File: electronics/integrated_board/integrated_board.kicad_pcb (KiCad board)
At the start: 2 copper layers, 98.5 x 111 mm, 67 parts, among them CON1 BARREL_JACK, J1 rot_encoderZ(35,34), J10 pcf8575 IO expander, J11 Switch 1, J13 motor1(15,2,0,4), J15 motor2 (16,17,5,18), J17 motor3 (19,21,22,23), J2 rot_encoderY(25,26), J3 rot_encoderX(14,27), J4 Switch 2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

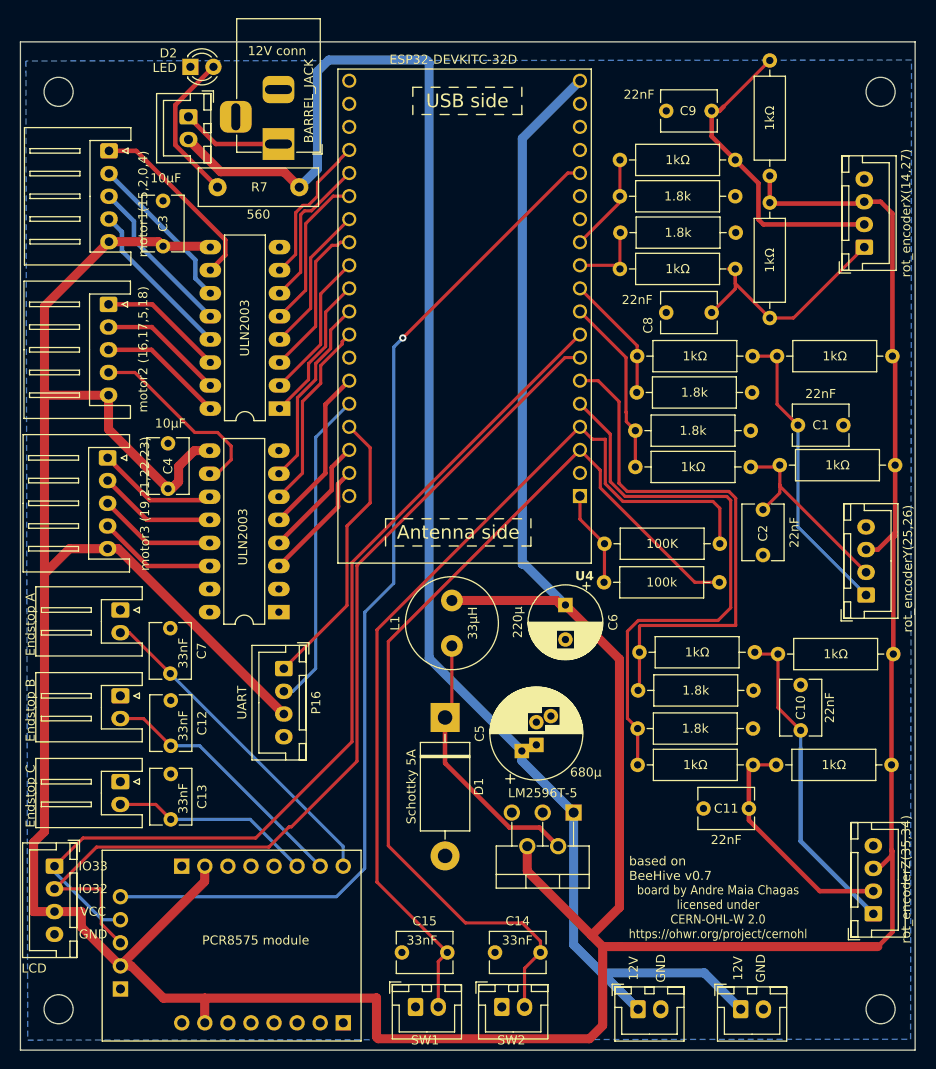
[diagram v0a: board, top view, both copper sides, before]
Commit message: Updated PCB
reintroduced voltage divider for switch 1 and 2 as pull up
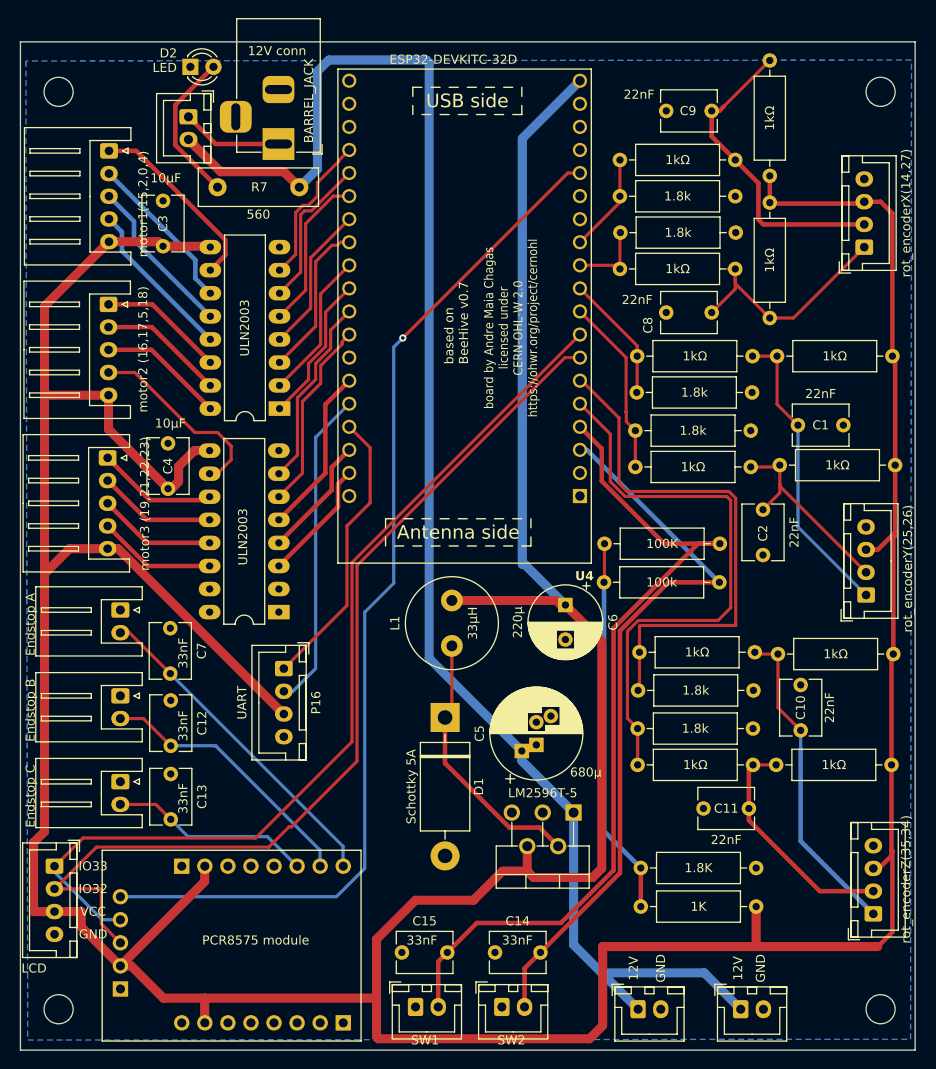
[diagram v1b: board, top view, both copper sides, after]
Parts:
- added R16: 1K, Resistor_THT:R_Axial_DIN0309_L9.0mm_D3.2mm_P12.70mm_Horizontal, F.Cu at (175.5, 135.2)
- added R17: 1.8K, Resistor_THT:R_Axial_DIN0309_L9.0mm_D3.2mm_P12.70mm_Horizontal, F.Cu at (162.8, 130.9)
- C14, C15: value C -> 33nF
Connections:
- R8 pad 2: +3V3 -> Net-(R16-Pad2)
- R9 pad 1: +3V3 -> Net-(R16-Pad2)
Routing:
- net Net-(R16-Pad2): track 0.00 -> 41.6 mm
- net Net-(J4-Pin_2): track 103.9 -> 80.3 mm
- net +5V: track 517.4 -> 535.6 mm
- net +3V3: track 10.6 -> 0.00 mm
- net Net-(J11-Pin_2): track 102.6 -> 93.5 mm
- net encoderZ_1: track 59.5 -> 58.5 mm
- net Net-(J6-Pin_2): track 28.7 -> 29.7 mm

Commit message: Updated endstop protocol
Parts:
- J10: moved to F.Cu
- moved J10 10.3 mm to (105.5, 134.0)
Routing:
- net +5V: track 535.6 -> 552.7 mm
- net I2C_SCL: track 103.7 -> 113.0 mm
- net I2C_INT: track 115.4 -> 119.6 mm
- net I2C_SDA: track 106.6 -> 105.6 mm

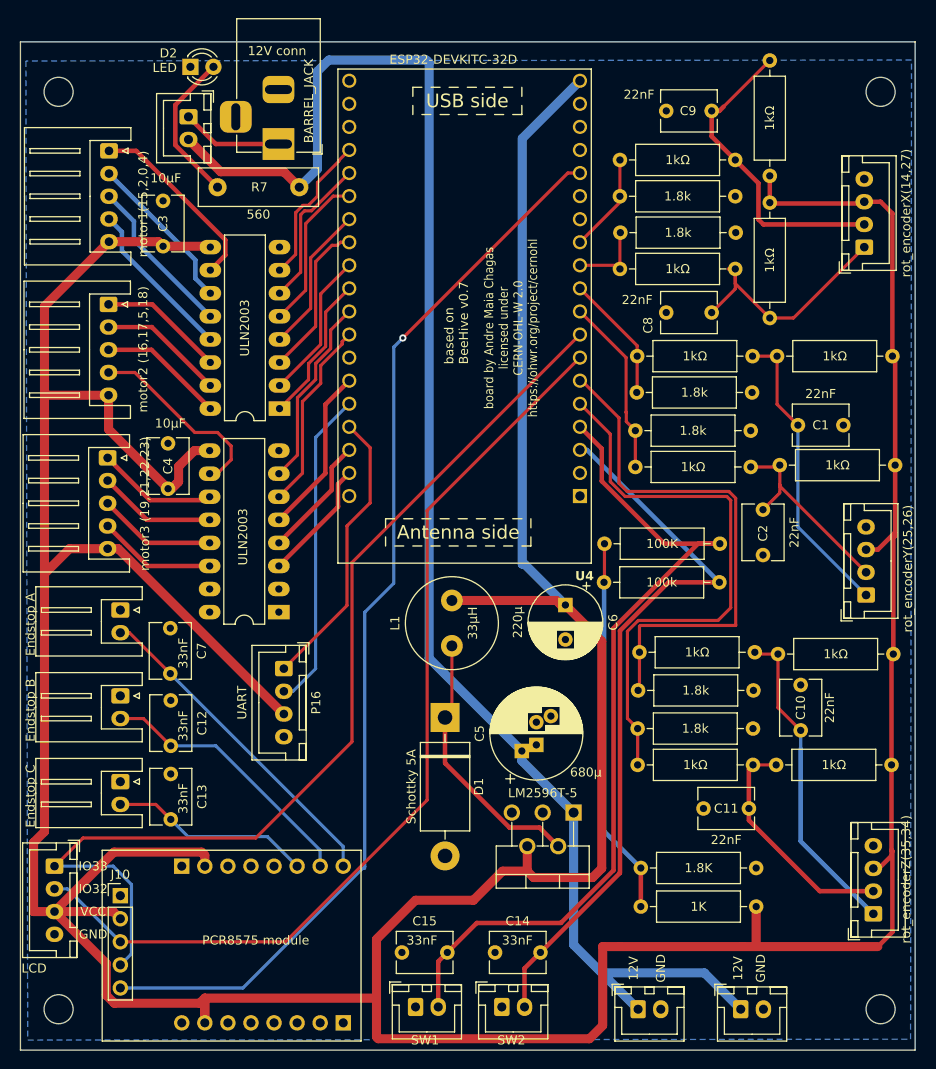
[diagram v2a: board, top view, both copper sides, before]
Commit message: Updated integrated PCB
- fixed footprint for pcf8575
- updated footprint for rotary encoder connectors for ease of use
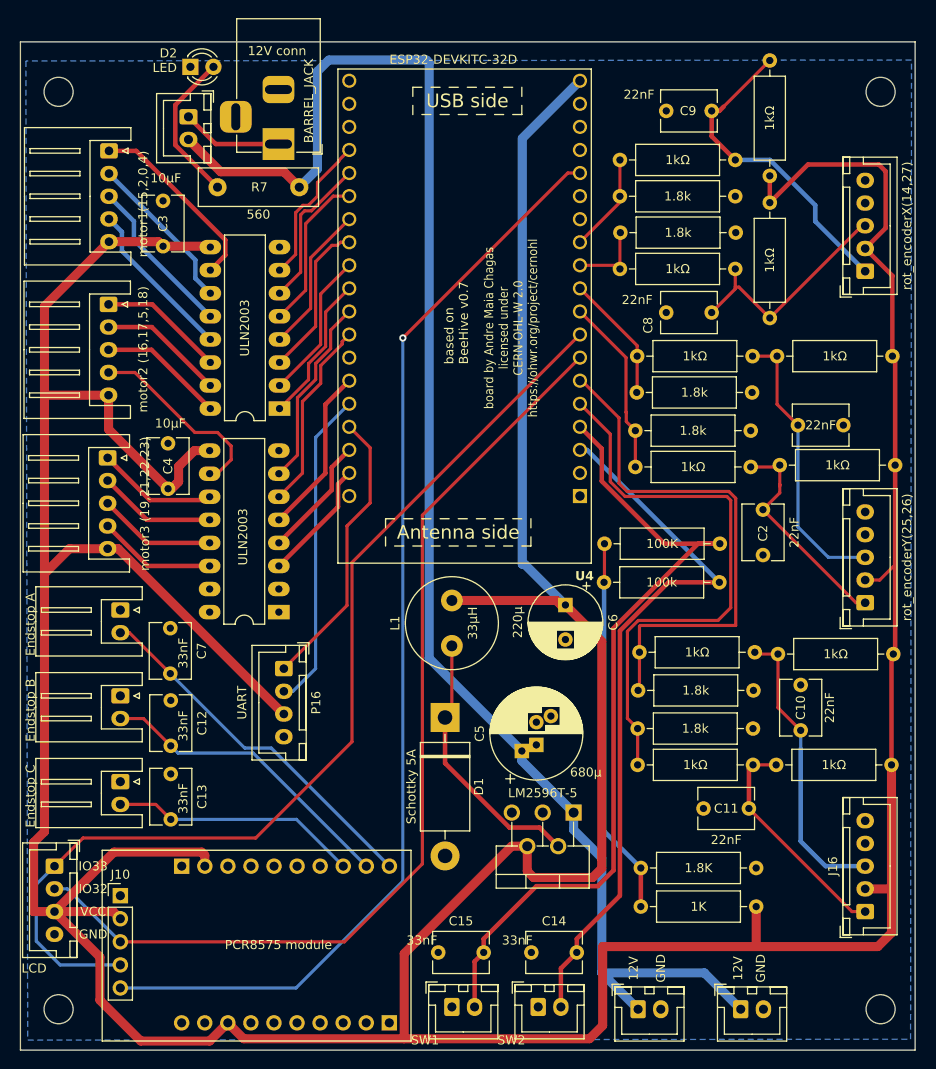
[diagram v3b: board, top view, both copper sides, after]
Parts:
- removed J1: rot_encoderZ(35,34), Connector_JST:JST_XH_B4B-XH-A_1x04_P2.50mm_Vertical
- removed J2: rot_encoderY(25,26), Connector_JST:JST_XH_B4B-XH-A_1x04_P2.50mm_Vertical
- removed J3: rot_encoderX(14,27), Connector_JST:JST_XH_B4B-XH-A_1x04_P2.50mm_Vertical
- added J12: rot_encoderX(14,27), Connector_JST:JST_XH_B5B-XH-A_1x05_P2.50mm_Vertical, F.Cu at (187.5, 65.2)
- added J14: rot_encoderY(25,26), Connector_JST:JST_XH_B5B-XH-A_1x05_P2.50mm_Vertical, F.Cu at (187.5, 101.8)
- added J16: rot_encoderZ(35,34), Connector_JST:JST_XH_B5B-XH-A_1x05_P2.50mm_Vertical, F.Cu at (187.5, 135.8)
- C12, C13, C7: value C -> 33nF
- J8, J9: footprint Connector_PinHeader_2.54mm:PinHeader_1x08_P2.54mm_Vertical -> Connector_PinHeader_2.54mm:PinHeader_1x10_P2.54mm_Vertical
- moved J8 5.07 mm to (135.1, 148.0)
- moved C14 4.00 mm to (150.8, 140.2)
- moved C15 4.00 mm to (140.5, 140.2)
- moved J11 4.00 mm to (142.0, 146.2)
- moved J4 4.00 mm to (151.5, 146.2)
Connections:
- J8 pad 7: +5V -> unconnected-(J8-Pin_7-Pad7)
- J8 pad 8: GND -> +5V
- J9 pad 6: Net-(J7-Pin_2) -> unconnected-(J9-Pin_6-Pad6)
- J9 pad 7: Net-(J6-Pin_2) -> unconnected-(J9-Pin_7-Pad7)
- J9 pad 8: Net-(J5-Pin_2) -> Net-(J7-Pin_2)
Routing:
- net Net-(J7-Pin_2): track 22.3 -> 27.4 mm
- net Net-(J6-Pin_2): track 29.7 -> 34.1 mm
- net Net-(J5-Pin_2): track 36.4 -> 40.3 mm
- net I2C_SDA: track 105.6 -> 109.4 mm
- net I2C_INT: track 119.6 -> 122.8 mm
- net Net-(J11-Pin_2): track 93.5 -> 90.4 mm
- net Net-(J16-Pin_3): track 35.6 -> 32.5 mm
- net +5V: track 552.7 -> 555.3 mm
- net Net-(J14-Pin_1): track 22.5 -> 24.6 mm
- net Net-(J14-Pin_3): track 33.1 -> 31.2 mm
- net Net-(J4-Pin_2): track 80.3 -> 78.7 mm
- net Net-(J12-Pin_3): track 27.3 -> 25.8 mm
- net Net-(J12-Pin_1): track 36.1 -> 37.0 mm
- net I2C_SCL: track 113.0 -> 113.7 mm
- net Net-(J16-Pin_1): track 25.8 -> 25.0 mm

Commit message: update enclosure
- updated design to avoid clashing footprints in the board / enclosure
- updated gerbers
-added some illustration images
-updated README
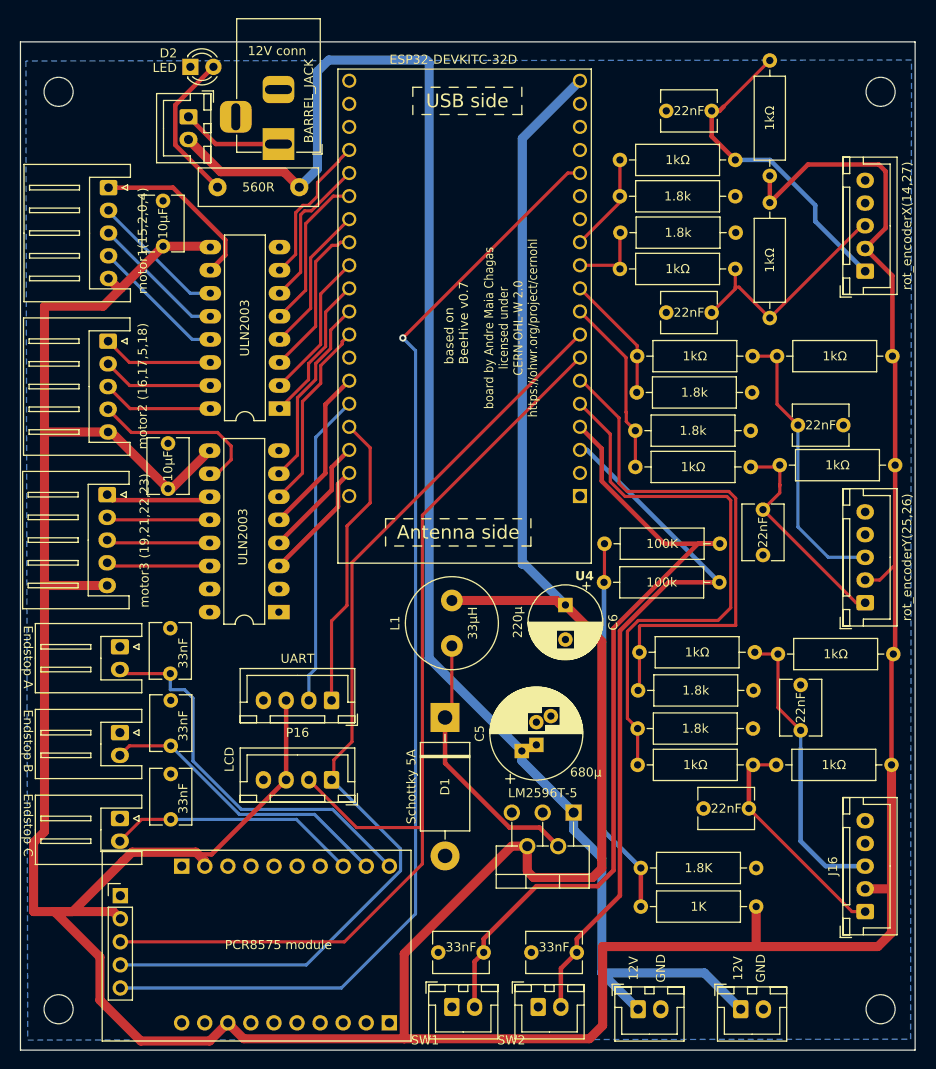
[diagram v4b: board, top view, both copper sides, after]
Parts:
- R7: value 560 -> 560R
- moved P2 31.9 mm to (128.8, 121.2), turned to 180 degrees
- moved P16 6.31 mm to (128.8, 112.5), turned to 180 degrees
- moved J13 4.05 mm to (104.2, 56.0)
- moved J15 4.05 mm to (104.2, 73.0)
- moved J17 4.05 mm to (104.0, 89.8)
- moved J5 4.05 mm to (105.5, 106.6)
- moved J6 4.05 mm to (105.5, 116.0)
- moved J7 4.05 mm to (105.5, 125.5)
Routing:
- net I2C_SCL: track 113.7 -> 108.5 mm
- net I2C_SDA: track 109.4 -> 114.4 mm
- net I2C_INT: track 122.8 -> 126.9 mm
- net Net-(J5-Pin_2): track 40.3 -> 43.7 mm
- net Net-(J13-Pin_4): track 17.9 -> 15.0 mm
- net Net-(J13-Pin_3): track 17.8 -> 15.0 mm
- net Net-(J13-Pin_2): track 17.8 -> 15.1 mm
- net +5V: track 555.3 -> 552.8 mm
- net Net-(J13-Pin_1): track 20.9 -> 19.2 mm
- net Net-(J17-Pin_4): track 13.1 -> 11.4 mm
- net Net-(J15-Pin_1): track 13.9 -> 12.2 mm
- net Net-(J17-Pin_3): track 13.0 -> 11.4 mm
- net Net-(J17-Pin_1): track 13.3 -> 11.7 mm
- net Net-(J15-Pin_3): track 13.9 -> 12.3 mm
- net Net-(J17-Pin_2): track 13.0 -> 11.4 mm
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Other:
- board text removed: "IO32"
- board text removed: "IO33"
- board text removed: "VCC"

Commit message: Documentation updated
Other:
- board text added: "GND VCC SDA SCL"
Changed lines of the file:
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@@
 		)
 		(fp_text user "${REFERENCE}"
-			(at 3.75 2.7 360)
+			(at 3.75 2.7 0)
 			(layer "F.Fab")
 			(effects
@@
 		(tags "connector JST XH vertical")
 		(property "Reference" "P16"
-			(at 3.75 -3.55 360)
+			(at 3.75 -3.55 0)
 			(layer "F.SilkS")
 			(effects
@@
 		)
 		(property "Value" "UART"
-			(at 3.75 4.6 360)
+			(at 3.75 4.6 0)
 			(layer "F.SilkS")
 			(effects
@@
 		)
 		(fp_text user "${REFERENCE}"
-			(at 3.75 2.7 360)
+			(at 3.75 2.7 0)
 			(layer "F.Fab")
 			(effects
@@
 		)
 	)
+	(gr_text "GND\nVCC\nSDA\nSCL"
+		(at 129.5 128 90)
+		(layer "F.SilkS")
+		(effects
+			(font
+				(size 1.5 1.5)
+				(thickness 0.3)
+				(bold yes)
+			)
+			(justify left bottom)
+		)
+	)

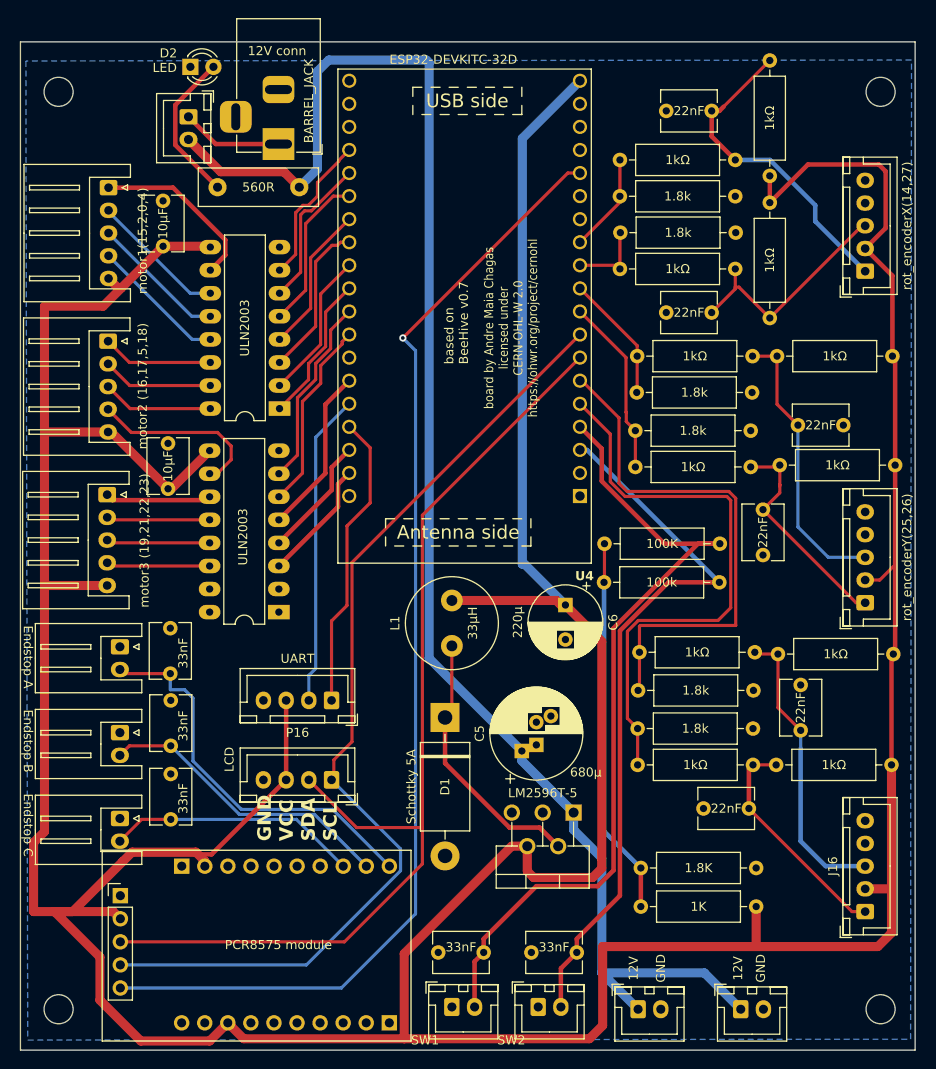
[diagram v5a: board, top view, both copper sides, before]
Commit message: Added BNC connectors to board
Intended as receivers of trigger signal for Z-stack
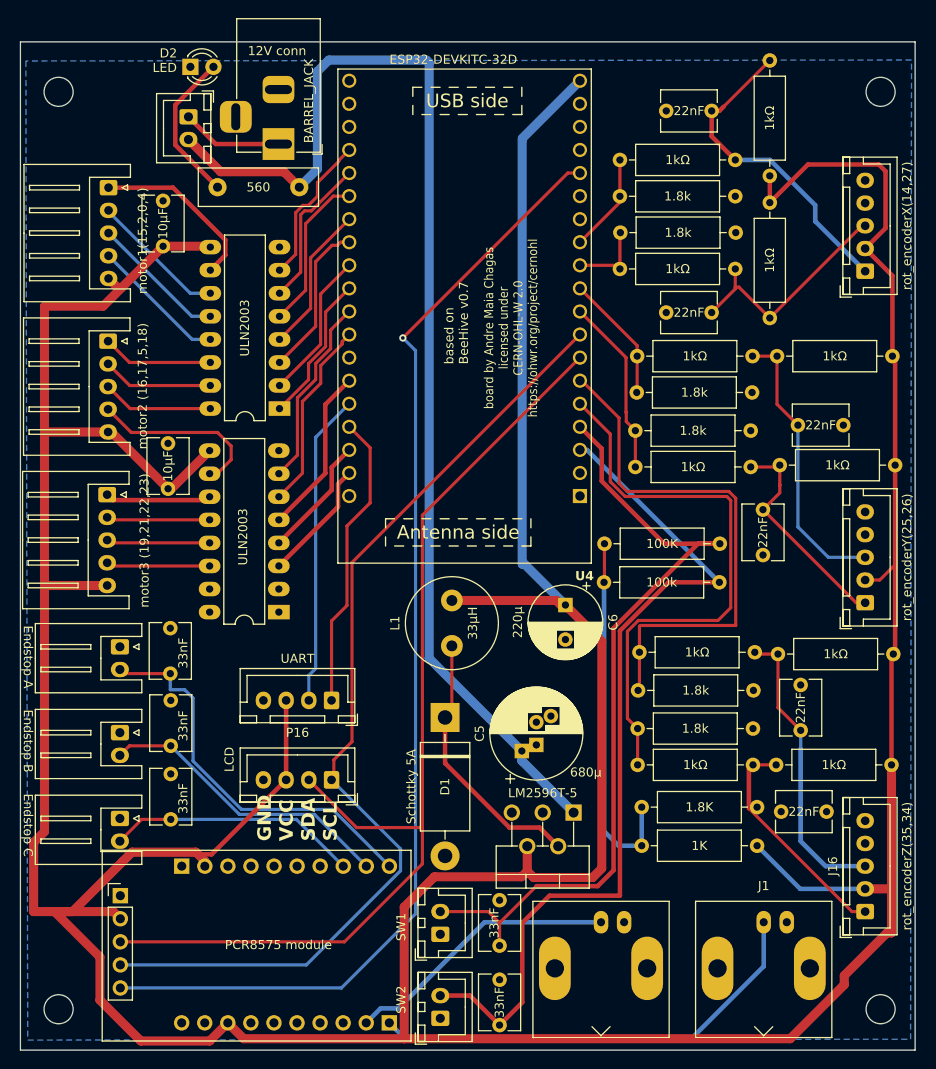
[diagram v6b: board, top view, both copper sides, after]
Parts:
- removed P10, P15: Conn_01x02, Connector_JST:JST_XH_B2B-XH-A_1x02_P2.50mm_Vertical
- added J1: Conn_Coaxial, Connector_Coaxial:BNC_Amphenol_B6252HB-NPP3G-50_Horizontal, F.Cu at (176.3, 136.9)
- added J2: Conn_Coaxial, Connector_Coaxial:BNC_Amphenol_B6252HB-NPP3G-50_Horizontal, F.Cu at (158.4, 136.9)
- R7: value 560R -> 560
- moved J4 10.8 mm to (140.7, 147.5), turned to 90 degrees
- moved C15 8.87 mm to (147.2, 134.5), turned to -90 degrees
- moved C11 8.56 mm to (178.2, 124.8)
- moved J11 8.10 mm to (140.7, 138.2), turned to 90 degrees
- moved R16 6.70 mm to (175.6, 128.5)
- moved R17 6.70 mm to (162.9, 124.2)
- moved C14 4.61 mm to (147.2, 143.2), turned to -90 degrees
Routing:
- net unconnected-(J1-In-Pad1): track 0.00 -> 50.1 mm
- net Net-(P1-Pin_2): track 171.6 -> 130.0 mm
- net unconnected-(J2-In-Pad1): track 0.00 -> 30.4 mm
- net Net-(J4-Pin_2): track 78.7 -> 95.9 mm
- net +5V: track 552.8 -> 559.7 mm
- net Net-(R16-Pad2): track 41.6 -> 40.7 mm
- net Net-(J11-Pin_2): track 90.4 -> 89.5 mm
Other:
- board text removed: "12V"
- board text removed: "GND"
